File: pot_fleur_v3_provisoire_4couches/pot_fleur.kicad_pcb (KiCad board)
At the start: 4 copper layers, 30 x 60 mm, 50 parts, among them J1 Conn_01x04_Pin, J10 P-MFC, J19 Conn_01x02_Socket, J2 Conn_01x04_Pin, J3 Conn_Coaxial_Small, J4 Conn_01x04_Pin, J5 Conn_01x02_Pin, J6 Conn_01x02_Pin, J7 Conn_01x04_Pin, SW1 B3U-1000P, SW2 B3U-1000P, U1 RAK3172-xx-8-SM-xI, U3 BQ25570, U4 SHT40-AD1B-R2

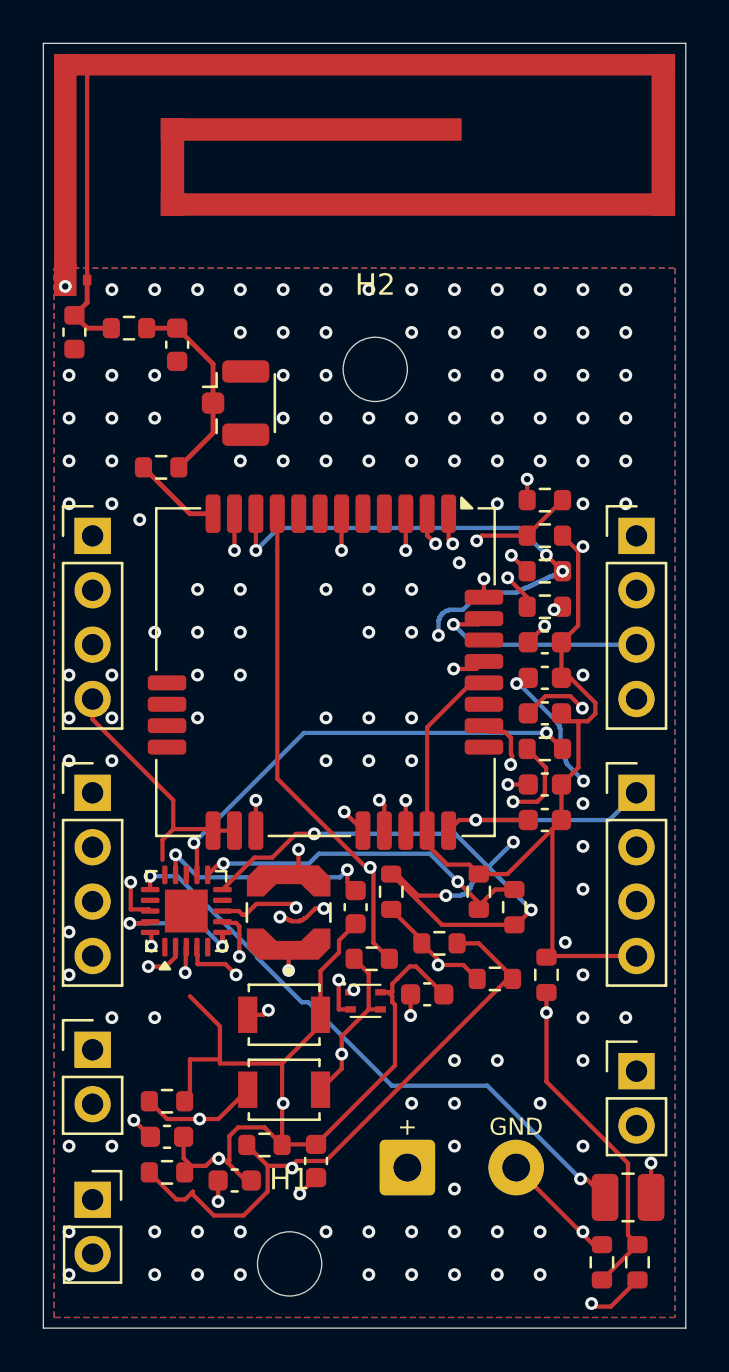
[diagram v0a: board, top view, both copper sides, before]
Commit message: Straighten V3 traces and remove redundant pad fragments
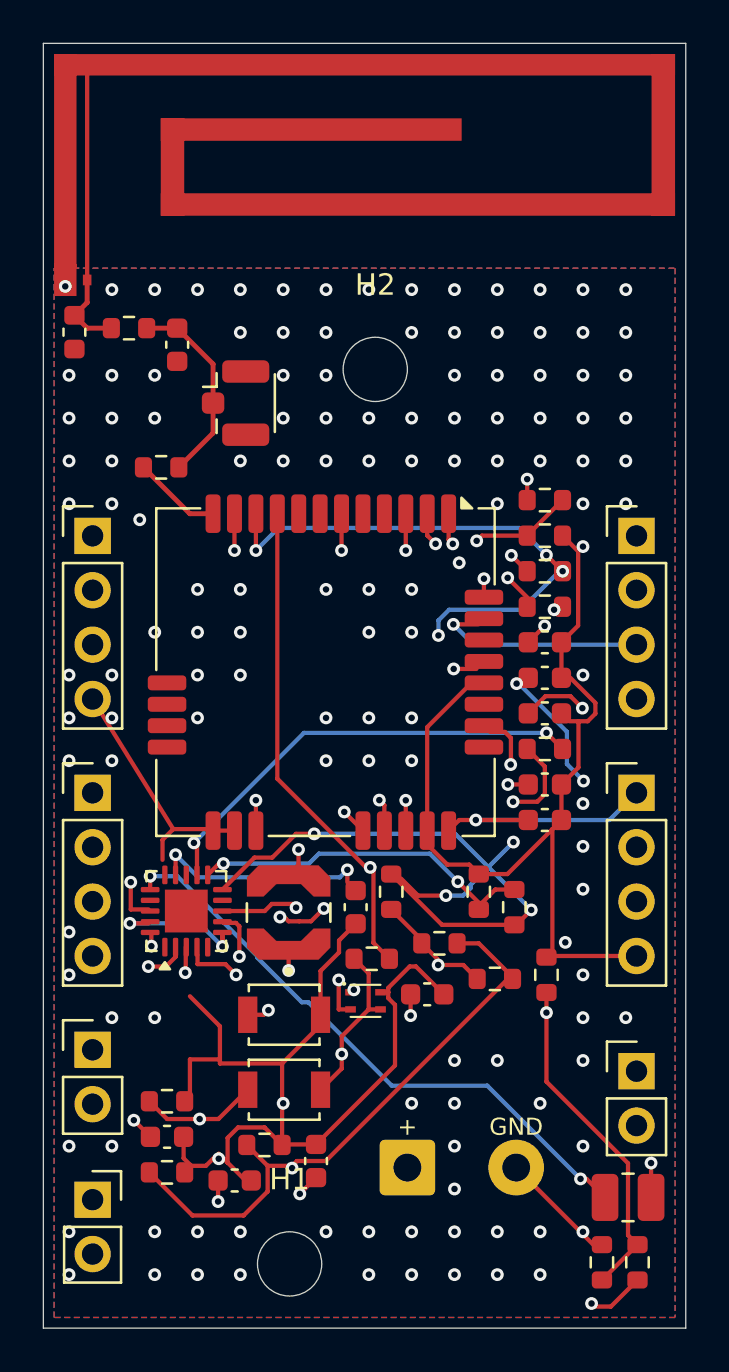
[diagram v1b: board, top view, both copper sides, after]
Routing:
- net GND: track 177.9 -> 172.8 mm
- net PA0: track 27.6 -> 25.8 mm
- net PB2: track 19.9 -> 18.4 mm
- net PWR: track 87.9 -> 86.4 mm
- net Net-(U3-OK_HYST): track 65.8 -> 64.6 mm
- net Net-(U3-VREF_SAMP): track 31.1 -> 30.1 mm
- net Net-(U3-VBAT_OV): track 41.4 -> 40.4 mm
- net /BQ25570/VRDIV: track 65.2 -> 64.4 mm
- net Net-(J6-Pin_1): track 41.3 -> 40.5 mm
- net PB5: track 15.4 -> 14.7 mm

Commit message: Remove obsolete ground spur from former UFL location
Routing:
- net GND: track 172.8 -> 164.8 mm
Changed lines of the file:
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@@
-	)
-	(segment
-		(start 56.845 97.45)
-		(end 58.2452 97.45)
-		(width 0.2)
-		(layer "F.Cu")
-		(net "GND")
 	)
 	(segment
@@
 	)
 	(segment
-		(start 58.2452 97.45)
-		(end 58.2452 95.9002)
-		(width 0.2)
-		(layer "F.Cu")
-		(net "GND")
-	)
-	(segment
 		(start 62.735 101.42)
 		(end 66.4225 97.7325)
@@
 	)
 	(segment
-		(start 58.2452 95.9002)
-		(end 56.845 94.5)
-		(width 0.2)
-		(layer "F.Cu")
-		(net "GND")
-	)
-	(segment
 		(start 75.7793 81.2996)
 		(end 75.4205 81.6584)
@@
 	)
 	(segment
-		(start 58.2452 97.6399)
-		(end 58.2452 97.45)
-		(width 0.2)
-		(layer "F.Cu")
-		(net "GND")
-	)
-	(segment
 		(start 58.925 86.765)
 		(end 57.925 86.765)
@@
 		(width 0.2)
 		(layer "F.Cu")
-		(net "GND")
-	)
-	(segment
-		(start 61.15 97.6399)
-		(end 58.2452 97.6399)
-		(width 0.2)
-		(layer "F.Cu")

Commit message: Audit every V3 trace and remove remaining ground stubs and via fragments
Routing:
- net GND: track 164.8 -> 161.2 mm
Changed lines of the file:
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@@
 	)
 	(segment
-		(start 58.0745 101.9718)
-		(end 58.0745 101.9716)
-		(width 0.2)
-		(layer "F.Cu")
-		(net "GND")
-	)
-	(segment
 		(start 64.585 91.115)
 		(end 63.8075 91.8925)
@@
 	)
 	(segment
-		(start 55.5642 88.1295)
-		(end 55.5642 87.197)
-		(width 0.2)
-		(layer "F.Cu")
-		(net "GND")
-	)
-	(segment
 		(start 59.0917 100.6264)
 		(end 60.3314 100.6264)
@@
 	)
 	(segment
-		(start 58.1897 102.087)
-		(end 58.0745 101.9718)
-		(width 0.2)
-		(layer "F.Cu")
-		(net "GND")
-	)
-	(segment
 		(start 57.5902 102.4203)
 		(end 56.9047 102.4203)
@@
 	)
 	(segment
-		(start 55.5642 87.197)
-		(end 56.0663 86.6949)
-		(width 0.2)
-		(layer "F.Cu")
-		(net "GND")
-	)
-	(segment
 		(start 63.8075 92.4548)
 		(end 62.945 93.3173)
@@
 	)
 	(segment
-		(start 56.845 99.16)
-		(end 56.845 97.45)
-		(width 0.2)
-		(layer "F.Cu")
-		(net "GND")
-	)
-	(segment
 		(start 74.9747 73.7197)
 		(end 74.9747 77.1903)
@@
 		(net "GND")
 	)
-	(segment
-		(start 58.0745 101.9718)
-		(end 58.0387 101.9718)
-		(width 0.2)
-		(layer "F.Cu")
-		(net "GND")
-	)
 	(via
 		(at 65.2 75.5)
@@
 	)
 	(segment
-		(start 69.1193 73.3224)
-		(end 69.1193 73.3745)
-		(width 0.2)
-		(layer "In1.Cu")
-		(net "UART2_RX")
-	)
-	(segment
 		(start 68.4548 72.6579)
 		(end 69.1193 73.3224)
@@
 	)
 	(segment
-		(start 66.925 73.6842)
-		(end 66.925 73.7892)
-		(width 0.2)
-		(layer "In1.Cu")
-		(net "PB5")
-	)
-	(segment
 		(start 63.925 71.965)
 		(end 63.925 73.6842)
@@
 	)
 	(segment
-		(start 65.2647 88.483)
-		(end 65.0672 88.483)
-		(width 0.2)
-		(layer "F.Cu")
-		(net "SCL")
-	)
-	(segment
 		(start 60.925 71.965)
 		(end 60.925 84.3408)
@@
 	)
 	(segment
-		(start 74.15 74.7)
-		(end 74.2 74.65)
-		(width 0.2)
-		(layer "B.Cu")
-		(net "SDA")
-	)
-	(segment
 		(start 74 74.75)
 		(end 74.05 74.75)
@@
 	)
 	(segment
-		(start 74.2 74.65)
-		(end 74.25 74.65)
-		(width 0.2)
-		(layer "B.Cu")
-		(net "SDA")
-	)
-	(segment
 		(start 68.45 77.65)
 		(end 68.45 76.95)
@@
 	)
 	(segment
-		(start 74.1 74.7)
-		(end 74.15 74.7)
-		(width 0.2)
-		(layer "B.Cu")
-		(net "SDA")
-	)
-	(segment
 		(start 74.05 74.75)
 		(end 74.1 74.7)
@@
 	)
 	(segment
-		(start 65.6171 85.2676)
-		(end 65.689 85.3395)
-		(width 0.2)
-		(layer "In2.Cu")
-		(net "BOOT")
-	)
-	(segment
 		(start 75.1715 81.0454)
 		(end 74.6131 80.487)
@@
 		(net "PB2")
 	)
-	(segment
-		(start 71.8239 83.6808)
-		(end 71.893 83.6117)
-		(width 0.2)
-		(layer "F.Cu")
-		(net "PB2")
-	)
 	(via
 		(at 71.8239 83.6808)
@@
 	)
 	(segment
-		(start 61.8023 90.1888)
-		(end 61.8023 90.3624)
-		(width 0.2)
-		(layer "F.Cu")
-		(net "/BQ25570/VRDIV")
-	)
-	(segment
 		(start 68.4363 93.0405)
 		(end 69.6105 93.0405)
@@
 	)
 	(segment
-		(start 72.15 79.9)
-		(end 72.2 79.85)
-		(width 0.2)
-		(layer "F.Cu")
-		(net "Net-(U3-VREF_SAMP)")
-	)
-	(segment
 		(start 62.5 91)
 		(end 63.1 90.4)
@@
 	)
 	(segment
-		(start 72.1 79.9)
-		(end 72.15 79.9)
-		(width 0.2)
-		(layer "F.Cu")
-		(net "Net-(U3-VREF_SAMP)")
-	)
-	(segment
 		(start 61.95 91)
 		(end 62.5 91)
@@
 	)
 	(segment
-		(start 61.05 90.8)
-		(end 61.25 90.8)
-		(width 0.2)
-		(layer "F.Cu")
-		(net "Net-(U3-VREF_SAMP)")
-	)
-	(segment
 		(start 61.3 90.85)
 		(end 61.45 91)
@@
 	)
 	(segment
-		(start 72.2 79.9)
-		(end 72.1 79.9)
-		(width 0.2)
-		(layer "B.Cu")
-		(net "Net-(U3-VREF_SAMP)")
-	)
-	(segment
 		(start 74.45 83.65)
 		(end 75.225 84.45)
@@
 	)
 	(segment
-		(start 54.0403 91.0942)
-		(end 54.0403 91.0943)
-		(width 0.2)
-		(layer "F.Cu")
-		(net "VOUT_EN")
-	)
-	(segment
 		(start 58.3625 91.52)
 		(end 58.3625 92.1772)
@@
 	)
 	(segment
-		(start 56.65 93.3)
-		(end 56.625 93.399999)
-		(width 0.2)
-		(layer "F.Cu")
-		(net "VOUT_EN")
-	)
-	(segment
 		(start 56.65 92.2)
 		(end 56.65 93.3)
@@
 	)
 	(segment
-		(start 56.625 93.399999)
-		(end 56.65 93.35)
-		(width 0.2)
-		(layer "In1.Cu")
-		(net "VOUT_EN")
-	)
-	(segment
 		(start 58.15 92.1)
 		(end 56.9 93.35)
@@
 	)
 	(segment
-		(start 73.4966 82.2016)
-		(end 73.4966 82.2)
-		(width 0.2)
-		(layer "F.Cu")
-		(net "Net-(U3-VOUT_SET)")
-	)
-	(segment
 		(start 74.245 82.95)
 		(end 73.4966 82.2016)
@@
 	)
 	(segment
-		(start 73.4966 82.2)
-		(end 73.495 82.2016)
-		(width 0.2)
-		(layer "In2.Cu")
-		(net "Net-(U3-VOUT_SET)")
-	)
-	(segment
 		(start 73.495 82.2016)
 		(end 73.495 95.2653)
@@
 	)
 	(segment
-		(start 56.175 87.8916)
-		(end 56.1762 87.8904)
-		(width 0.2)
-		(layer "F.Cu")
-		(net "Net-(J6-Pin_1)")
-	)
-	(segment
 		(start 64.1966 89.1766)
 		(end 64.1966 88.5973)
@@
 	)
 	(segment
-		(start 61.9681 103.7292)
-		(end 61.9758 103.7292)
-		(width 0.2)
-		(layer "In1.Cu")
-		(net "Net-(U3-VBAT)")
-	)
-	(segment
 		(start 55.206 101.271)
 		(end 59.5099 101.271)
@@
 		(width 0.2)
 		(layer "F.Cu")
-		(net "Net-(U3-VBAT_OV)")
-	)
-	(segment
-		(start 61.6156 102.4183)
-		(end 61.6156 102.5259)
-		(width 0.2)
-		(layer "F.Cu")
